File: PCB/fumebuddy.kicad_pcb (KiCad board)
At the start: 2 copper layers, 26.2 x 67.2 mm, 24 parts, among them J1 USB_B_Micro, J2 STATION, J3 esp32buddy, J4 TOUCH, SW1 SW_SPDT, SW2 SW_SPDT, SW3 FLASH, U1 AP7361C-33E, U2 CPC1017N (NO), U4 ESP32-WROOM-32D, U5 CPC1117N (NC)

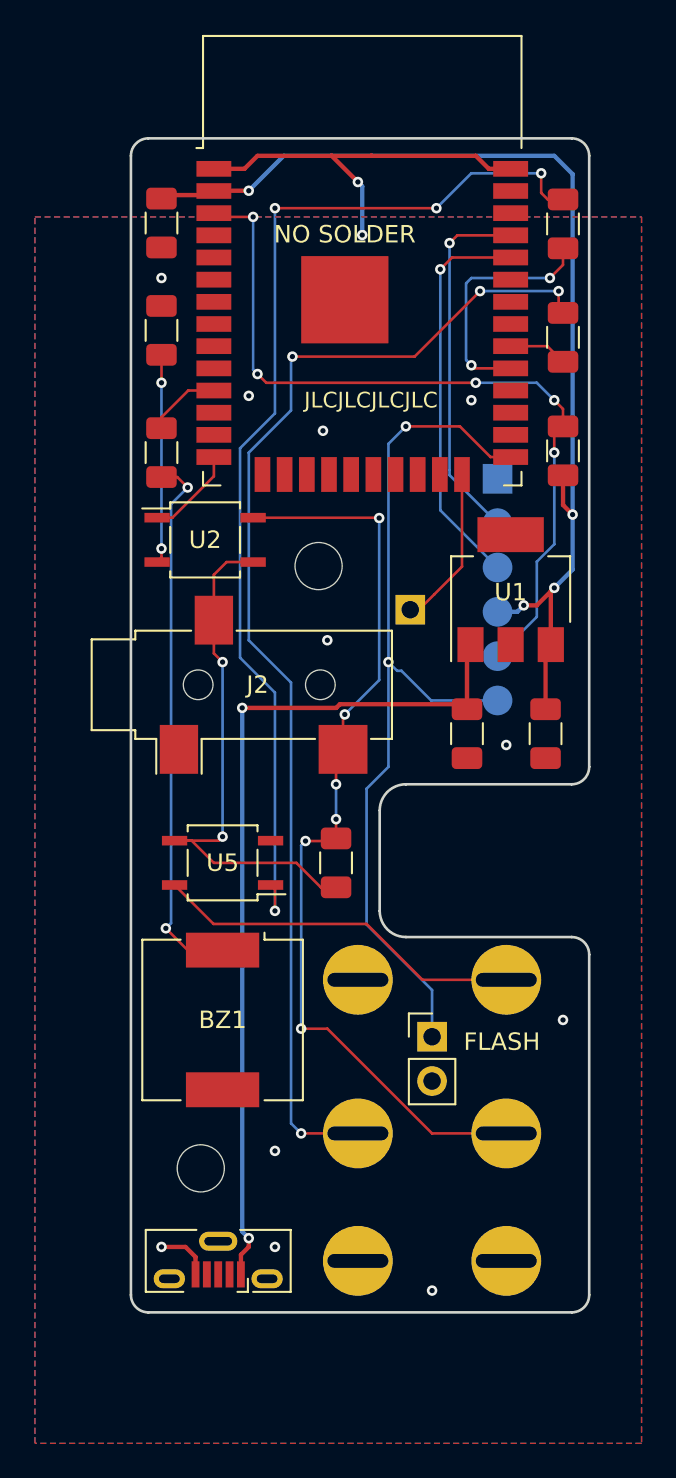
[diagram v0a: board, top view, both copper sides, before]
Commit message: Change programming header, no more flash header
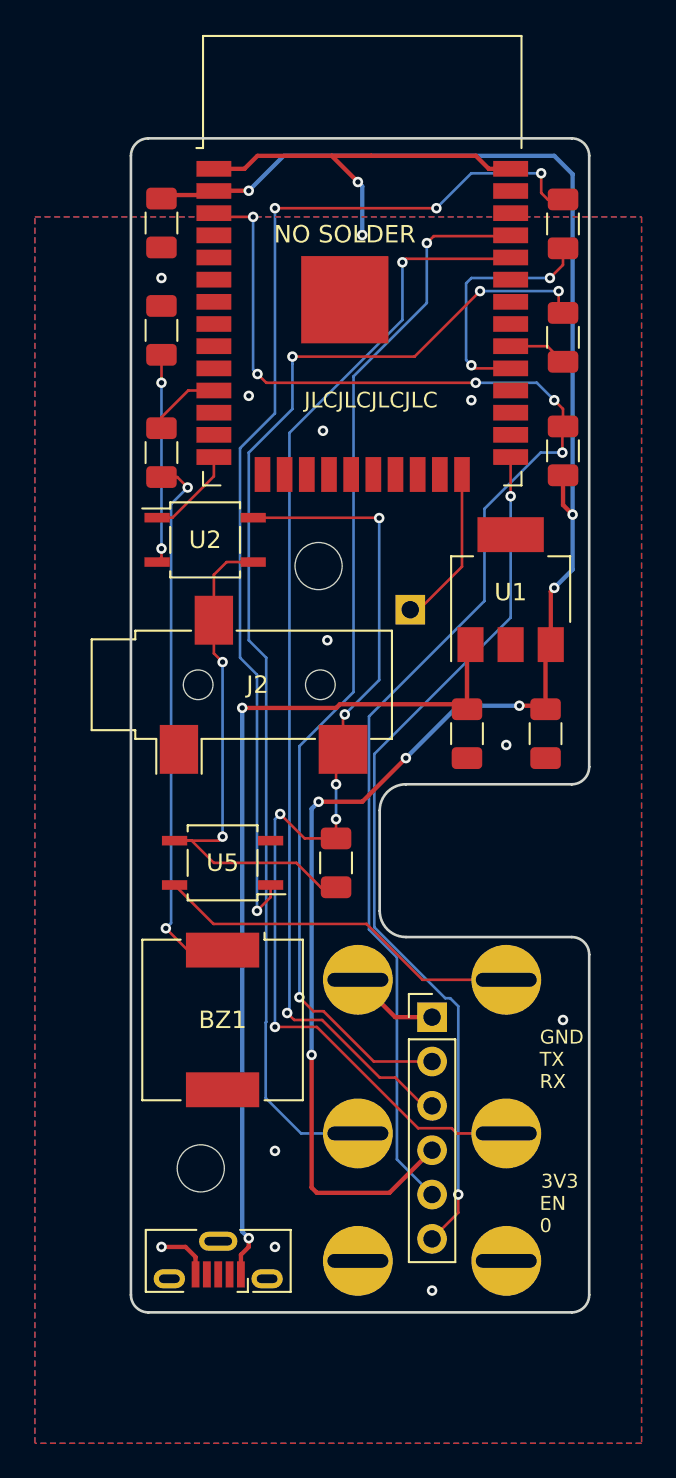
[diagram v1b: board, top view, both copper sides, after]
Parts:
- removed SW3: FLASH, Connector_PinHeader_2.54mm:PinHeader_1x02_P2.54mm_Vertical
- J3: footprint !Greg:esp32buddy-2.54mm -> !Greg:PinHeader_1x06_P2.54mm_Vertical; moved to F.Cu
- moved J3 31.1 mm to (131.0, 132.8), turned to 0 degrees
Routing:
- net +3V3: track 62.7 -> 104.8 mm, vias 4 -> 7
- net /RXD: track 22.7 -> 62.6 mm, vias 1 -> 2
- net /TXD: track 20.9 -> 60.3 mm, vias 1 -> 2
- net /EN: track 45.5 -> 82.3 mm
- net GND: track 26.2 -> 31.3 mm
- net Net-(J2-PadT): track 53.8 -> 58.7 mm
- net /GPIO0: track 51.3 -> 50.8 mm
- net Net-(R1-Pad2): vias 4 -> 3
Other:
- board text added: "fumebuddy v6"
- board text removed: "fumebuddy v5"

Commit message: updates
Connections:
- J1 pad 2: (no net) -> unconnected-(J1-D--Pad2)
- J1 pad 3: (no net) -> unconnected-(J1-D+-Pad3)
- J1 pad 4: (no net) -> unconnected-(J1-ID-Pad4)
- J1 pad 6: Net-(J1-Pad6) -> unconnected-(J1-Shield-Pad6)
- J2 pad S: (no net) -> unconnected-(J2-PadS)
- SW1 pad 3: (no net) -> unconnected-(SW1-C-Pad3)
- SW2 pad 3: (no net) -> unconnected-(SW2-C-Pad3)
- U4 pad 10: (no net) -> unconnected-(U4-IO25-Pad10)
- U4 pad 12: (no net) -> unconnected-(U4-IO27-Pad12)
- U4 pad 13: (no net) -> unconnected-(U4-IO14-Pad13)
- U4 pad 16: (no net) -> unconnected-(U4-IO13-Pad16)
- U4 pad 17: (no net) -> unconnected-(U4-SHD/SD2-Pad17)
- U4 pad 18: (no net) -> unconnected-(U4-SWP/SD3-Pad18)
- U4 pad 19: (no net) -> unconnected-(U4-SCS/CMD-Pad19)
- U4 pad 20: (no net) -> unconnected-(U4-SCK/CLK-Pad20)
- U4 pad 21: (no net) -> unconnected-(U4-SDO/SD0-Pad21)
- U4 pad 22: (no net) -> unconnected-(U4-SDI/SD1-Pad22)
- U4 pad 23: (no net) -> unconnected-(U4-IO15-Pad23)
- U4 pad 26: (no net) -> unconnected-(U4-IO4-Pad26)
- U4 pad 27: (no net) -> unconnected-(U4-IO16-Pad27)
- U4 pad 28: (no net) -> unconnected-(U4-IO17-Pad28)
- U4 pad 31: (no net) -> unconnected-(U4-IO19-Pad31)
- U4 pad 32: (no net) -> unconnected-(U4-NC-Pad32)
- U4 pad 33: (no net) -> unconnected-(U4-IO21-Pad33)
- U4 pad 36: (no net) -> unconnected-(U4-IO22-Pad36)
- U4 pad 37: (no net) -> unconnected-(U4-IO23-Pad37)
- U4 pad 4: (no net) -> unconnected-(U4-SENSOR_VP-Pad4)
- U4 pad 5: (no net) -> unconnected-(U4-SENSOR_VN-Pad5)
- U4 pad 6: (no net) -> unconnected-(U4-IO34-Pad6)
- U4 pad 7: (no net) -> unconnected-(U4-IO35-Pad7)
- U4 pad 8: (no net) -> unconnected-(U4-IO32-Pad8)
- U4 pad 9: (no net) -> unconnected-(U4-IO33-Pad9)
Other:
- net class Default removed
- net class Power removed
